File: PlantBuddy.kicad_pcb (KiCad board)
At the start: 4 copper layers, 44.3 x 29.2 mm, 77 parts, among them J1 USB_C_Receptacle_USB2.0, J101 JST, J102 Debug, J4 External, SW1 SW_Push, U1 LTR-303ALS-01, U101 AP2139AK-3.0TRG1, U102 nRF52832-QFAA, U104 XB5350A, U105 CN809T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

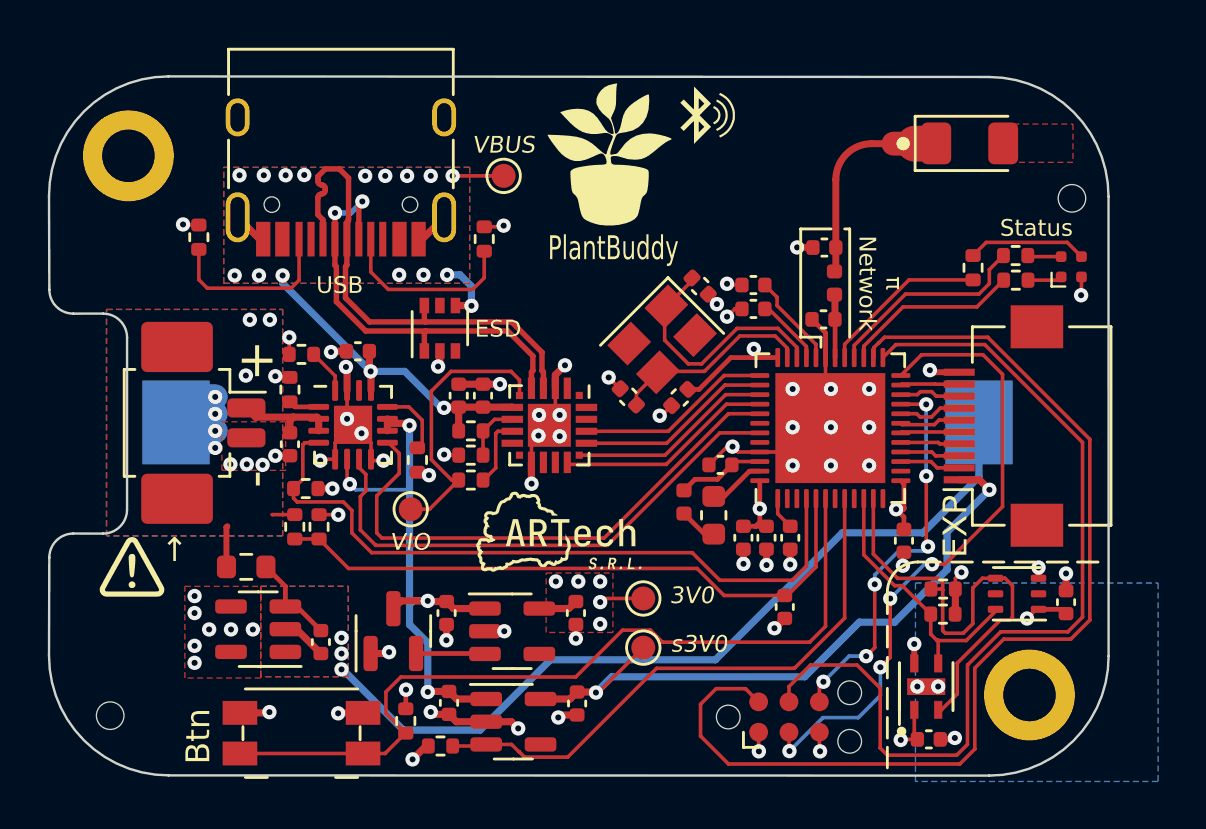
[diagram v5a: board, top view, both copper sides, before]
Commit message: Switched to single i2c bus.
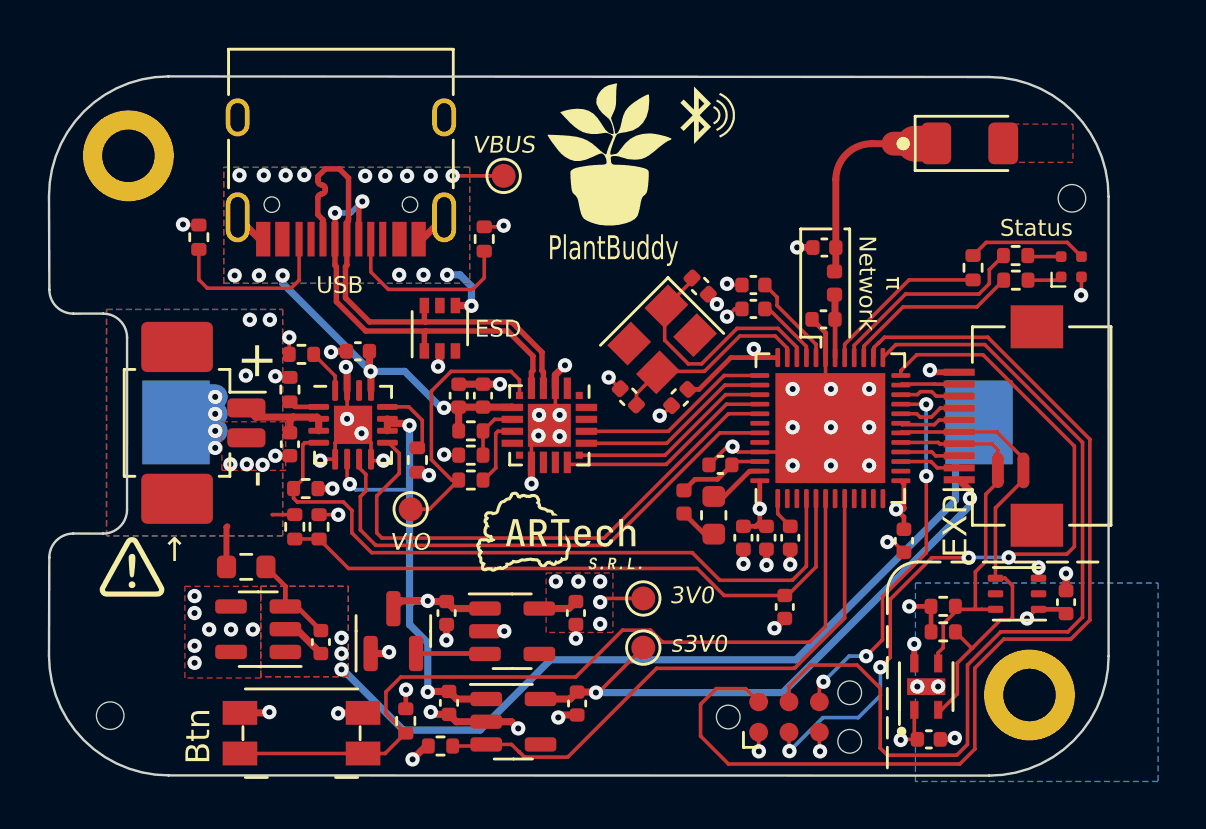
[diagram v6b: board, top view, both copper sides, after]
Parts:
- added NT101: NetTie_2, NetTie:NetTie-2_SMD_Pad0.5mm, F.Cu at (155.5, 129.3)
- added NT102: NetTie_2, NetTie:NetTie-2_SMD_Pad0.5mm, F.Cu at (156.6, 129.3)
- moved R3 1.79 mm to (153.2, 136.0), turned to 180 degrees
- moved R4 0.32 mm to (153.2, 135.0), turned to 180 degrees
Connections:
- U102 pad 10: /SDA -> unconnected-(U102-Pad10)
- U102 pad 11: /SCL -> unconnected-(U102-Pad11)
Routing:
- net /SCL: track 19.9 -> 13.2 mm
- net /~{tRST}: track 26.6 -> 31.9 mm
- net /EXT4: track 2.46 -> 5.60 mm
- net /S_3V0: track 27.5 -> 25.4 mm
- net /EXT3: track 2.47 -> 4.54 mm
- net /SDA: track 11.4 -> 9.89 mm
- net /SWO: track 16.5 -> 15.8 mm, vias 6 -> 4

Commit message: Changed antenna configuration back.
After testing I found out that this antenna configuration works
better.
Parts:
- H101, H104: value ToolingHole -> MountingHole; footprint Tooling:JLCPCB_Tooling_hole -> MountingHole:MountingHole_2.2mm_M2_DIN965_Pad
- moved AE101 5.58 mm to (148.7, 115.4), turned to 90 degrees
- moved H104 2.48 mm to (156.8, 116.2)
- moved H101 1.19 mm to (119.2, 138.7)
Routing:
- net /FEED: track 8.87 -> 4.23 mm
- removed copper zone on F.Cu, net /Trace

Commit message: Changed to IFA antenna
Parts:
- removed the G*** at (137.2, 131.8)
- removed the G*** at (139.3, 116.1)
- AE101: value Antenna_Chip -> Antenna_MIFA; footprint LED_SMD:LED_1206_3216Metric -> RF_Antenna:Texas_SWRA117D_2.4GHz_Left
- moved G*** 8.29 mm to (137.2, 120.0), turned to -90 degrees
- moved AE101 3.13 mm to (148.7, 118.5), turned to 0 degrees
- moved TP103 0.41 mm to (134.4, 117.0)
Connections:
- AE101 pad 2: /Trace -> GND
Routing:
- net /FEED: track 4.23 -> 2.53 mm
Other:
- board text removed: "EXP"
- board text removed: "PlantBuddy"
